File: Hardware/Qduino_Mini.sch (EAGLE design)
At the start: 39 parts, among them Q1 PFET, U1 ATMEGA32U41:1-LESS_PASTE, U2 MCP73831, U3 MAX17048, U4 AP2112K-3.3TRG-1, U5 MIGHTYQ-L-SILK, Y1 8MHZ

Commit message: Fixed PROD_ID on caps again
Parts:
- C1, C2: PROD_ID CAP-10300 -> CAP-08280
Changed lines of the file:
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@@
 </part>
 <part name="C2" library="SparkFun-Passives" deviceset="CAP" device="0603-CAP" value="4.7uF">
-<attribute name="PROD_ID" value="CAP-10300"/>
+<attribute name="PROD_ID" value="CAP-08280"/>
 </part>
 <part name="C1" library="SparkFun-Passives" deviceset="CAP" device="0603-CAP" value="4.7uF">
-<attribute name="PROD_ID" value="CAP-10300"/>
+<attribute name="PROD_ID" value="CAP-08280"/>
 </part>
 <part name="C4" library="SparkFun-Passives" deviceset="CAP" device="0603-CAP" value="1uF">

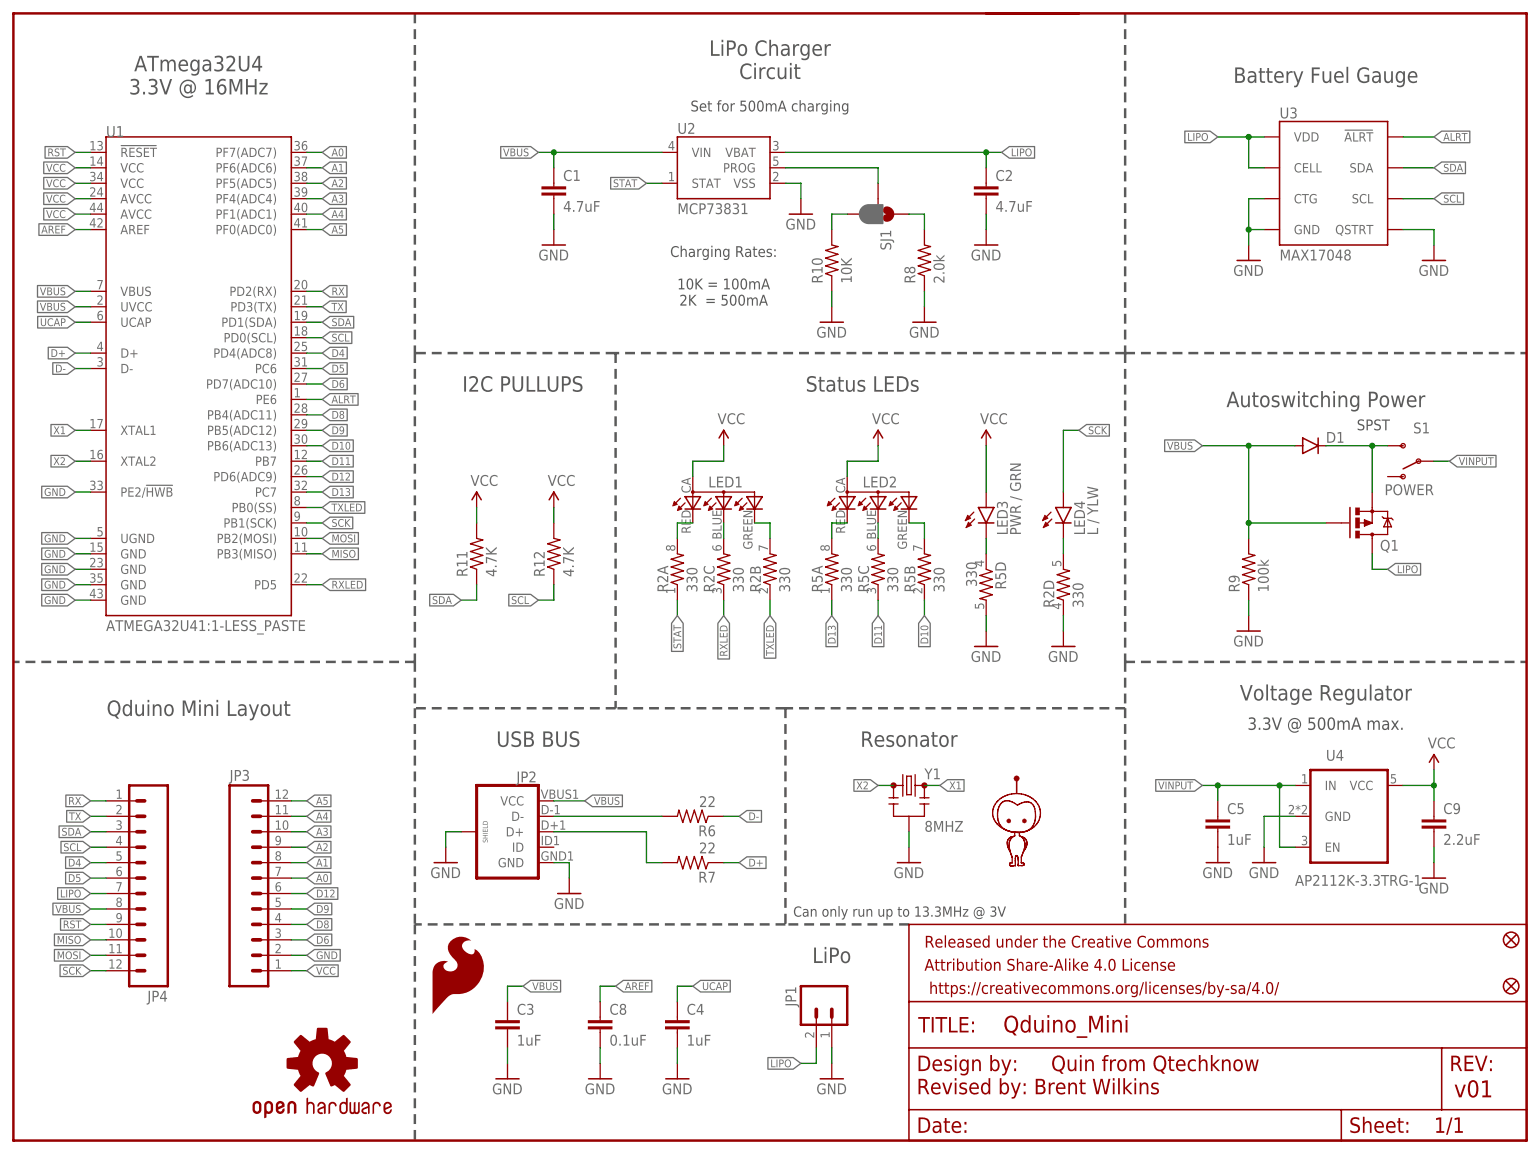
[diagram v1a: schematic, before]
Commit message: Renamed a few parts and removed gnd traces under gnd pours
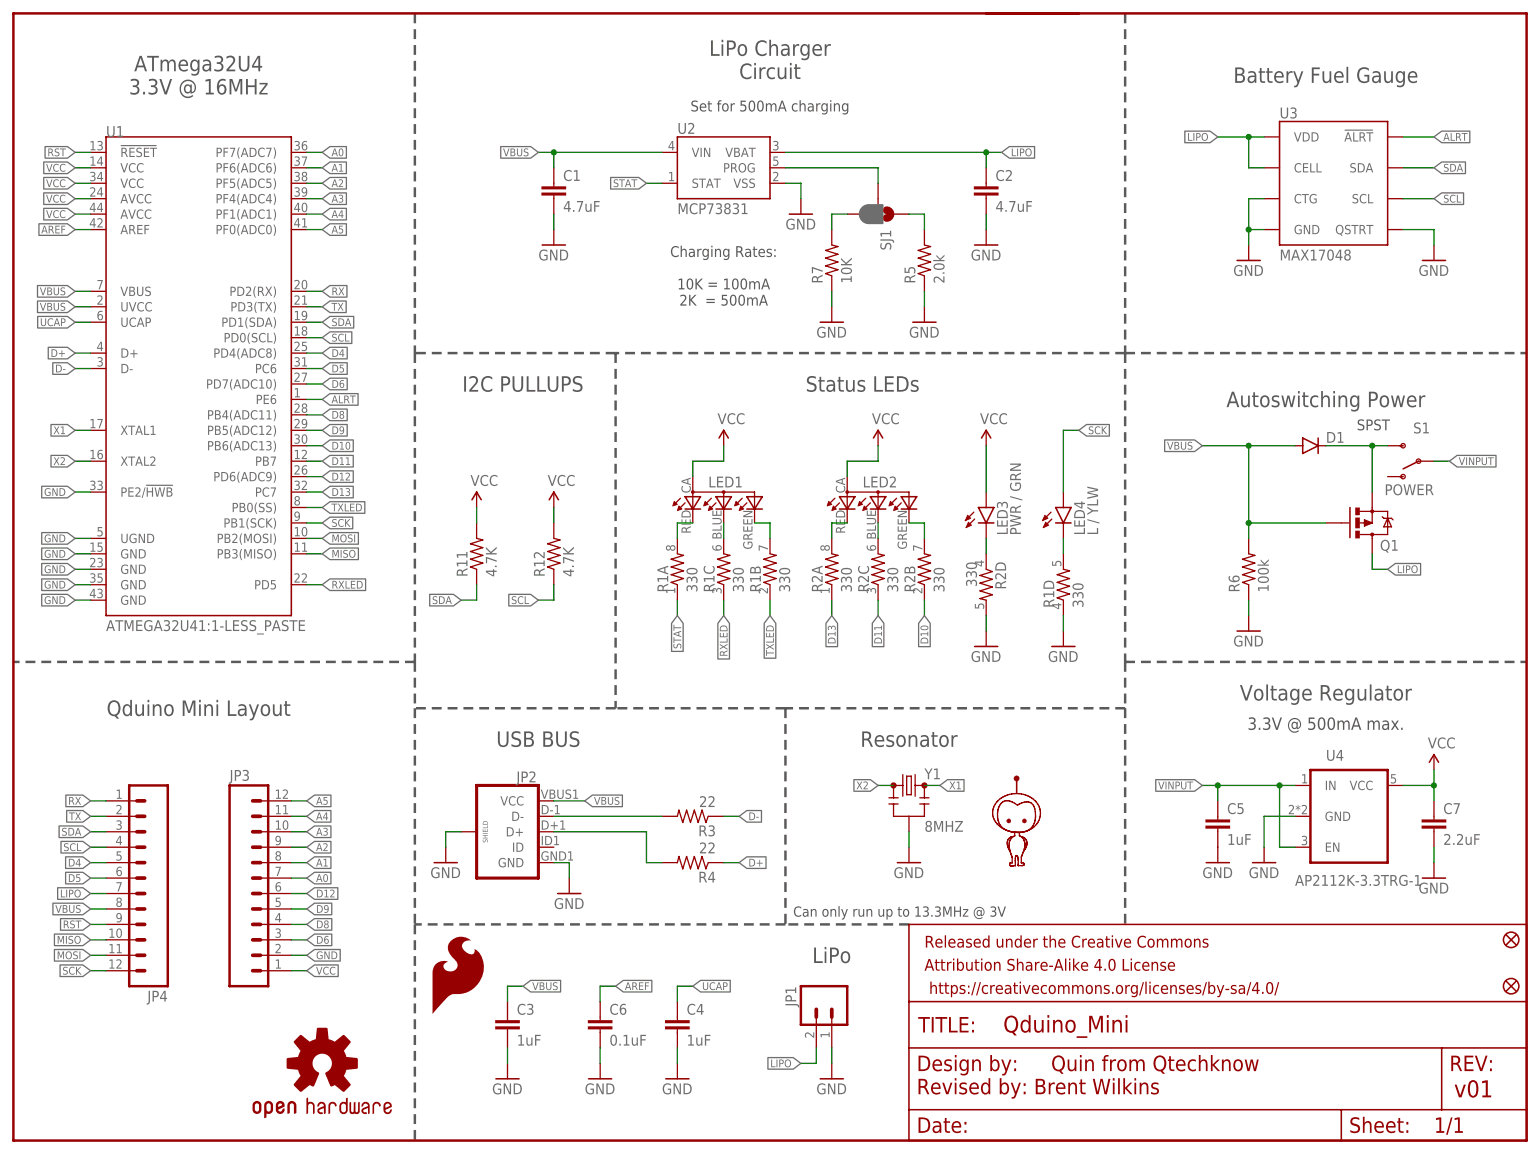
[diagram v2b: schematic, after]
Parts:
- removed R10: 10K, SparkFun-Resistors:10KOHM-1/10W-1%(0603)0603
- removed R8: 2.0k, SparkFun-Resistors:2.0KOHM1/10W5%(0603)
- removed R9: 100k, SparkFun-Resistors:100KOHM-1/10W-1%(0603)
- added R1: 330, SparkFun-Passives:RESISTOR-ARRAY0603-ARV
- added R3, R4: 22, SparkFun-Resistors:RESISTOR0603
- R5: value 330 -> 2.0k; device SparkFun-Passives:RESISTOR-ARRAY0603-ARV -> SparkFun-Resistors:2.0KOHM1/10W5%(0603)
- R6: value 22 -> 100k; device SparkFun-Resistors:RESISTOR0603 -> SparkFun-Resistors:100KOHM-1/10W-1%(0603); PROD_ID RES-08698 -> (none)
- R7: value 22 -> 10K; device SparkFun-Resistors:RESISTOR0603 -> SparkFun-Resistors:10KOHM-1/10W-1%(0603)0603; PROD_ID RES-08698 -> (none)
- renumbered C8 to C6, C9 to C7
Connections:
- net D+: now also R4.1; no longer R7.1
- net D-: now also R3.1; no longer R6.1
- net D10: now also R2B.1; no longer R5B.1
- net D11: now also R2C.1; no longer R5C.1
- net D13: now also R2A.1; no longer R5A.1
- net GND: now also R1D.1, R2D.2, R5.1, R6.1, R7.1; no longer R10.1, R2D.1, R5D.2, R8.1, R9.1
- net N$1: now also R1A.2; no longer R2A.2
- net N$2: now also R1C.2; no longer R2C.2
- net N$32: now also R2C.2; no longer R5C.2
- net N$34: now also R1B.2; no longer R2B.2
- net N$35: now also R2A.2; no longer R5A.2
- net N$37: now also R2B.2; no longer R5B.2
- net N$4: now also R2D.1; no longer R5D.1
- net N$5: now also R1D.2; no longer R2D.2
- net N$6: now also R7.2; no longer R10.2
- net N$7: now also R5.2; no longer R8.2
- net RXLED: now also R1C.1; no longer R2C.1
- net STAT: now also R1A.1; no longer R2A.1
- net TXLED: now also R1B.1; no longer R2B.1
- net UD+: now also R4.2; no longer R7.2
- net UD-: now also R3.2; no longer R6.2
- net VBUS: now also R6.2; no longer R9.2
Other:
- moved on the sheet: R2A, R2B, R2C, R2D, R6, R7

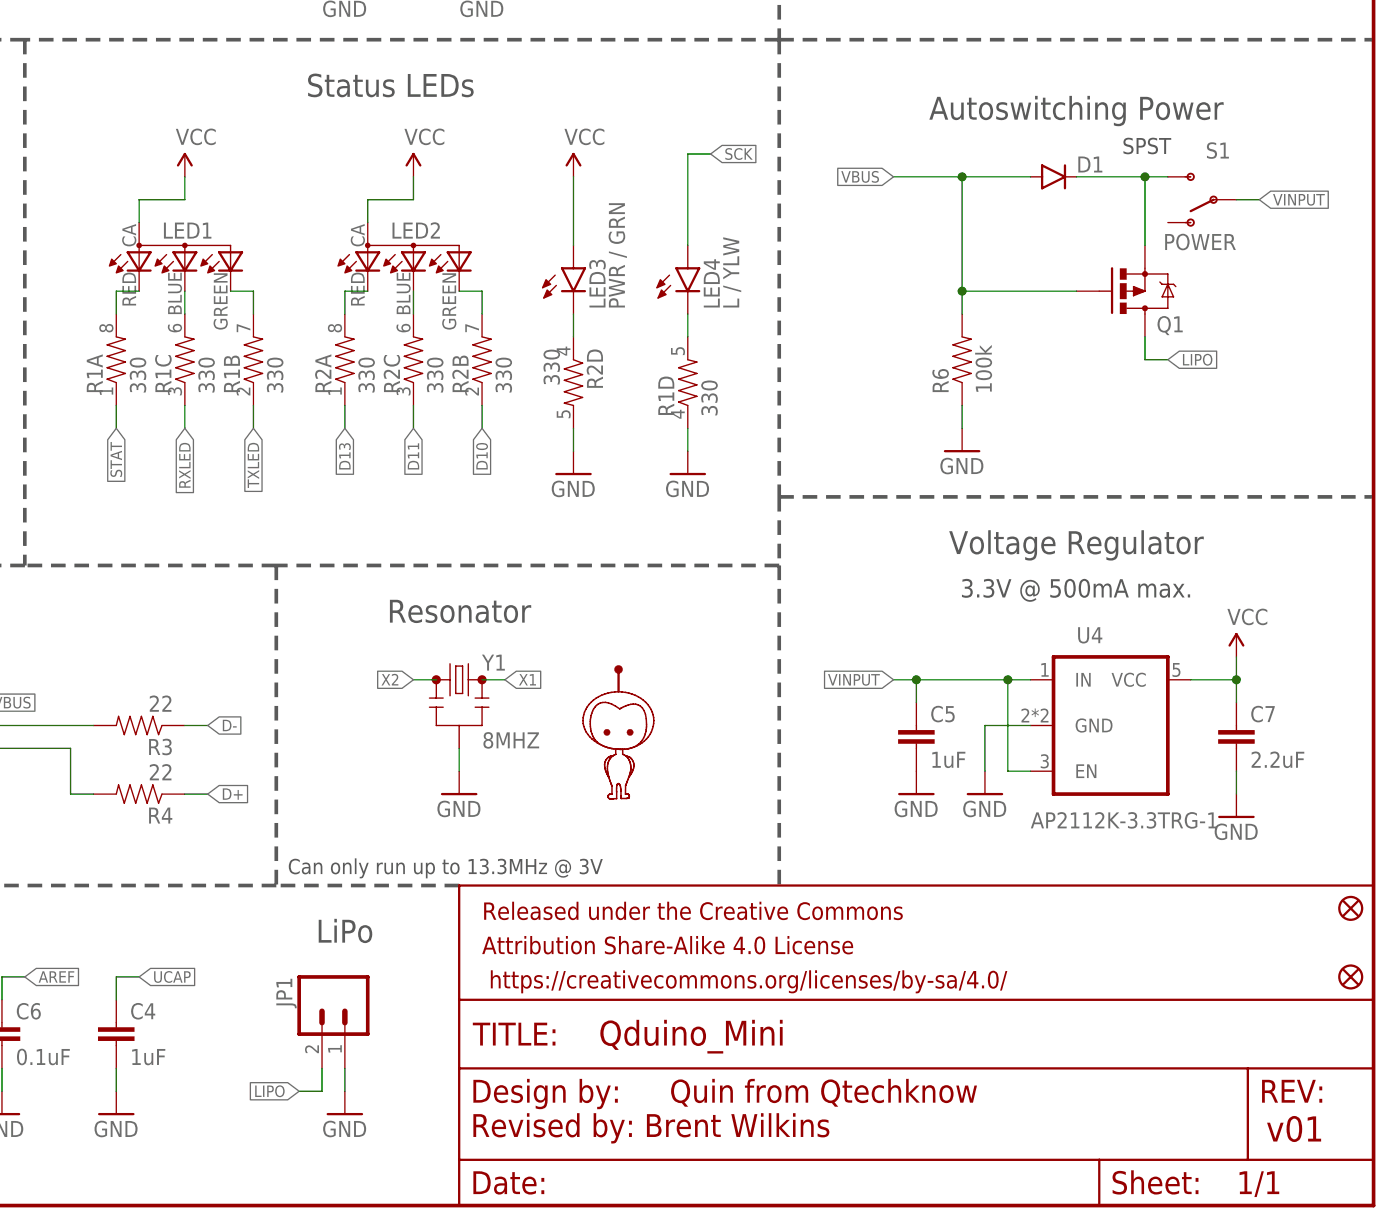
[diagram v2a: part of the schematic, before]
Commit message: Converted more parts to parts SFE uses
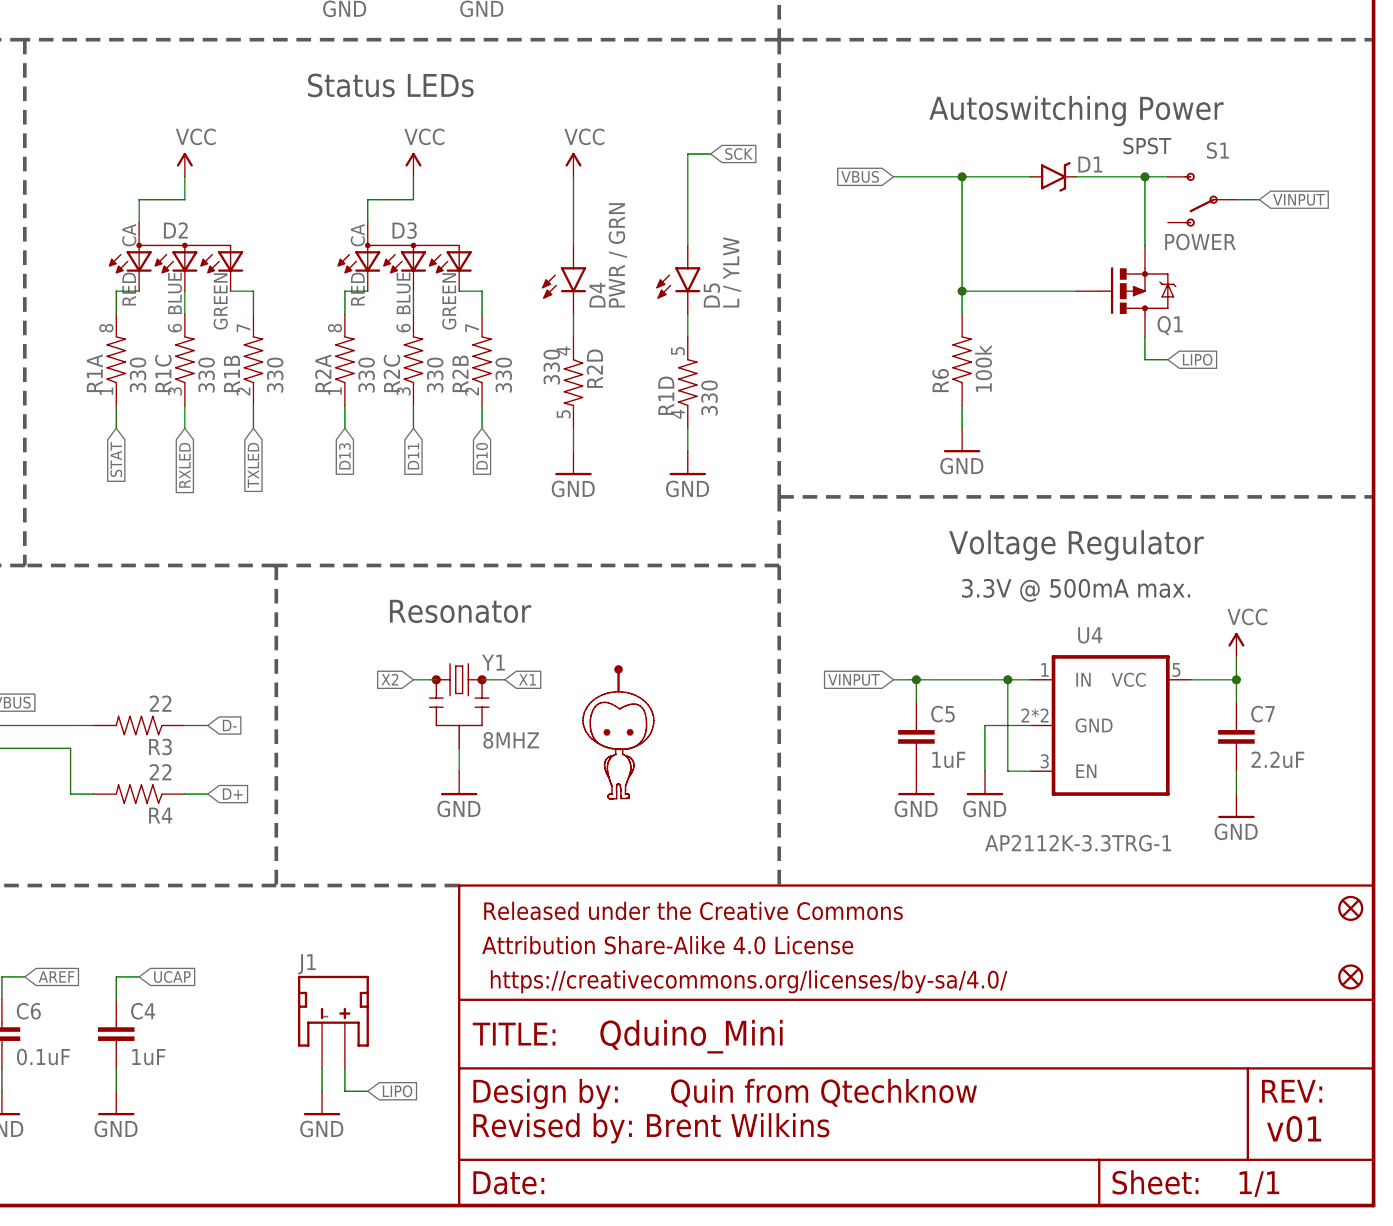
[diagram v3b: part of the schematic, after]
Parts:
- removed JP1: LiPo, SparkFun:M02-JST-2MM-SMT
- added J1: LiPo, SparkFun-Connectors:JST_2MM_MALE
- D1: value 250mA/100V -> BAT20J; device SparkFun-DiscreteSemi:DIODEBAS16 -> SparkFun-DiscreteSemi:DIODE-SCHOTTKY-BAT20J
- renumbered LED1 to D2, LED2 to D3, LED3 to D4, LED4 to D5
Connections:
- net GND: now also J1.-; no longer JP1.1
- net LIPO: now also J1.+; no longer JP1.2
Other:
- note removed: "Can only run up to 13.3MHz @ 3V"
